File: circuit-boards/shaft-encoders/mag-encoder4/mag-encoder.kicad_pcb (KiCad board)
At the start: 4 copper layers, 19.9 x 27.8 mm, 25 parts, among them J1 CONFIG, J2 0015912055, U1 AP2120N-3.3TRG1, U2 SN74LVC7032ABQAR, U3 MA732GQ

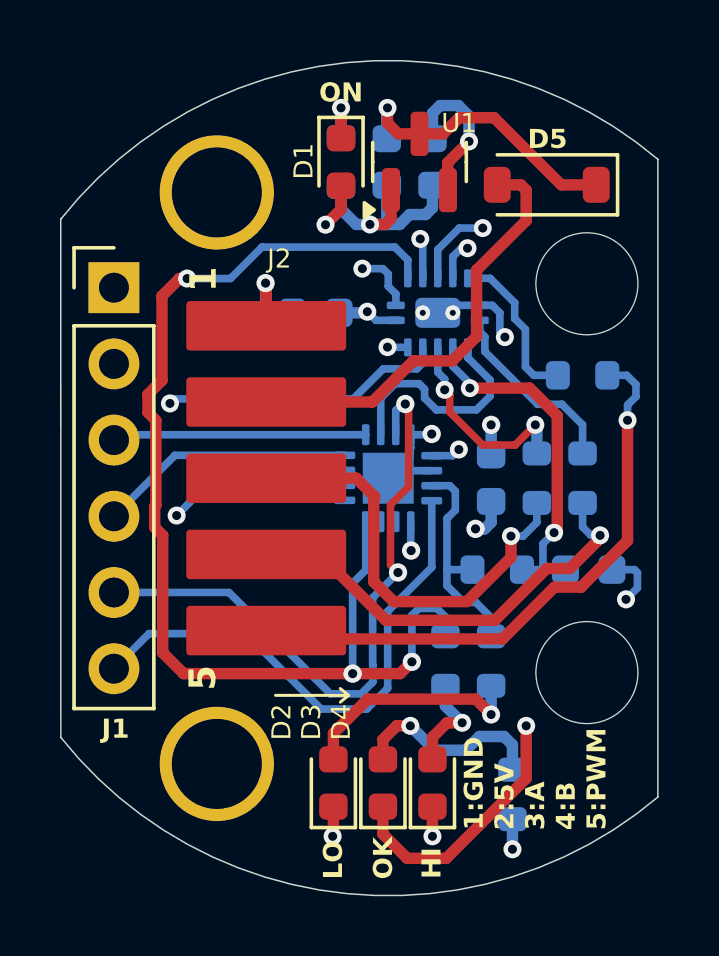
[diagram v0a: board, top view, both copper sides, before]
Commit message: Minor layout fix to mag encoder
Signed-off-by: scott <sgberman1@gmail.com>
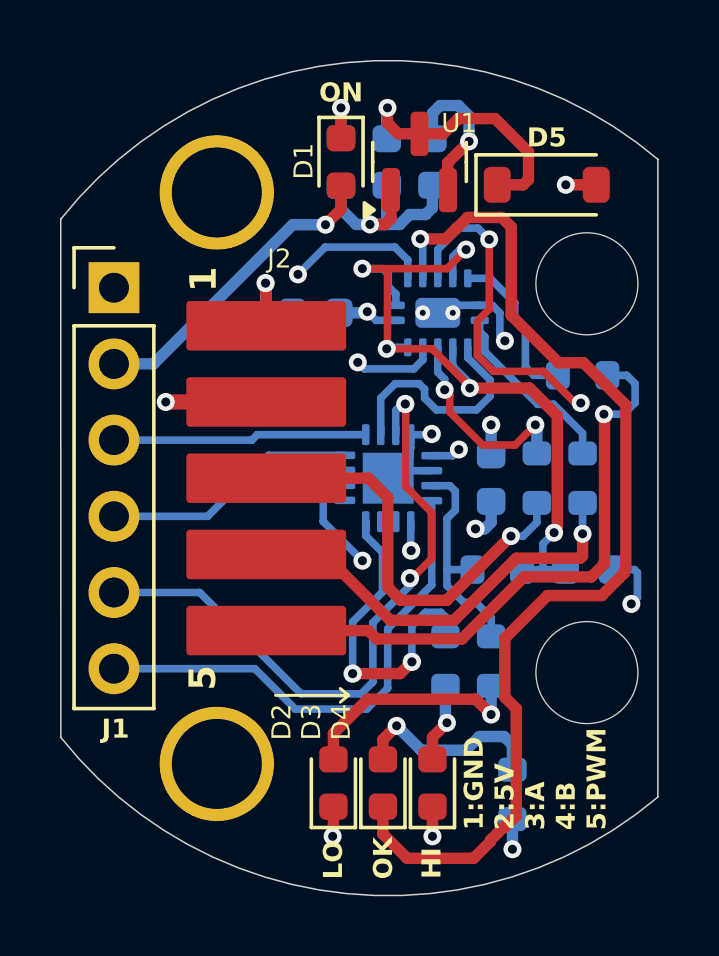
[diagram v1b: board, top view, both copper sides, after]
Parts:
- turned D5 to 0 degrees
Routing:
- net +5V_IN: track 14.5 -> 4.36 mm, vias 0 -> 2
- net Net-(U3-MGH): track 39.5 -> 30.2 mm
- net +3.3V: track 12.0 -> 21.0 mm
- net Net-(U3-A): track 19.4 -> 14.0 mm
- net Net-(U3-PWM): track 11.9 -> 17.0 mm, vias 2 -> 3
- net Net-(D3-K): track 32.1 -> 35.7 mm, vias 2 -> 1
- net Net-(C1-Pad1): track 27.2 -> 25.7 mm
- net /SCLK: track 17.8 -> 16.8 mm
- net /PWM: track 19.9 -> 20.7 mm
- net Net-(D4-A): track 3.39 -> 2.67 mm
- net +5V: track 9.80 -> 9.10 mm
- net /B: track 14.8 -> 14.1 mm
- added copper zone on In1.Cu, net +5V_IN

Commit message: Change Green LED current to 5mA
Signed-off-by: scott <sgberman1@gmail.com>
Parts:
- R5: value 1.00k-1%-0603 -> 249R-1%-0603
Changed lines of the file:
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@@
 		(tags "SOD-123")
 		(property "Reference" "D5"
-			(at 0 -1.5748 360)
+			(at 0 -1.5748 0)
 			(layer "F.SilkS")
 			(effects
@@
 		)
 		(property "Value" "MMSD4148T1G"
-			(at 0 2.1 360)
+			(at 0 2.1 0)
 			(layer "F.Fab")
 			(effects
@@
 		)
 		(fp_text user "${REFERENCE}"
-			(at 0 -2 360)
+			(at 0 -2 0)
 			(layer "F.Fab")
 			(effects
@@
 			)
 		)
-		(property "Value" "1.00k-1%-0603"
+		(property "Value" "249R-1%-0603"
 			(at 0 -1.43 90)
 			(layer "B.Fab")
@@
 			)
 		)
-		(property "DIST P/N" "311-1.00KHRCT-ND"
+		(property "DIST P/N" "311-249HRCT-ND"
 			(at 0 0 90)
 			(unlocked yes)
@@
 			)
 		)
-		(property "MFG P/N" "RC0603FR-071KL"
-			(at 0 0 90)
-			(unlocked yes)
+		(property "MFG P/N" "RC0603FR-07249RL"
+			(at 0 0 90)
+			(unlocked yes)

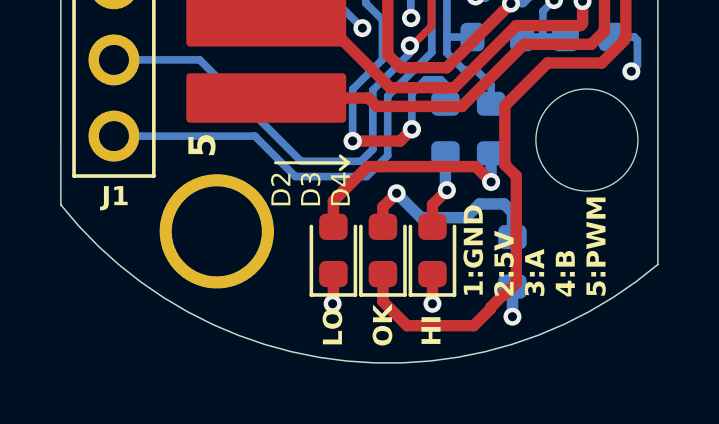
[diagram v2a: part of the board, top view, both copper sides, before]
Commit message: Update mag encoder silk and board color
Signed-off-by: scott <sgberman1@gmail.com>
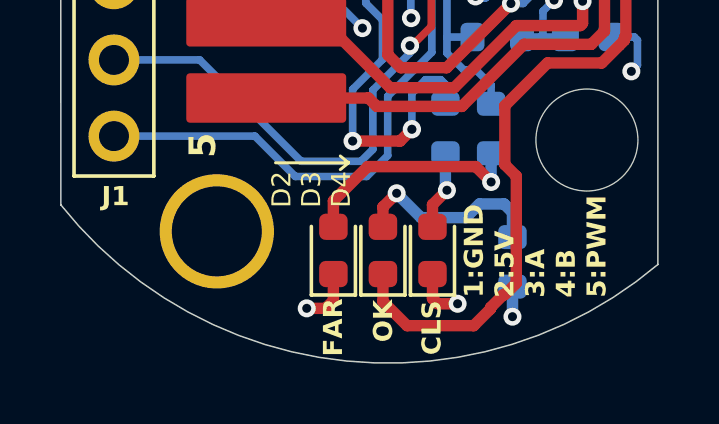
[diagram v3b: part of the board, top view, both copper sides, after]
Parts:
- D2: value LO -> FAR
- D4: value HI -> CLS
- R8: value 1.00k-1%-0603 -> 249R-1%-0603
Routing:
- net GND: track 24.1 -> 25.7 mm
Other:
- board text added: "Blue"
- board text added: "NOTES: 1. LAYERS: 4 2. PCB THICKNESS: 1.6mm 3. PCB COLOR: BLUE 4. SILKSCREEN: WHITE 5. MATERIAL TYPE: FR4 TG-155 6. SURFACE FINISH: ENIG 7. OUTER COPPER WEIGHT: 1oz 8. INNER COPPER WEIGHT: 0.5oz 9. IMPEDANCE CONTROL: NO 10. VIA COVERING: PLUGGED 11. MIN VIA HOLE DIA: 0.2mm 12. BOARD OUTLINE TOLERANCE: +/-0.2mm"
- board text removed: "Green"
- board text removed: "NOTES: 1. LAYERS: 4 2. PCB THICKNESS: 1.6mm 3. PCB COLOR: GREEN 4. SILKSCREEN: WHITE 5. MATERIAL TYPE: FR4 TG-155 6. SURFACE FINISH: ENIG 7. OUTER COPPER WEIGHT: 1oz 8. INNER COPPER WEIGHT: 0.5oz 9. IMPEDANCE CONTROL: NO 10. VIA COVERING: PLUGGED 11. MIN VIA HOLE DIA: 0.2mm 12. BOARD OUTLINE TOLERANCE: +/-0.2mm"
